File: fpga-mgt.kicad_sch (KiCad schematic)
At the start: 1 part, among them U1 XC7K410T-2FFG900I

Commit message: Loclib
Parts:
- U1: footprint antmicro-footprints:xc7k410t-2ffg900I -> K410T-devboard-footprints:xc7k410t-2ffg900I; symbol antmicroMicrocontrollers:XC7K410T-2FFG900I -> K410T-devboard:XC7K410T-2FFG900I

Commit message: Bump revision to 1.0.0. Update name on schematic and PCB sheets
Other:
- title: K410T devboard -> Kintex 410T devboard

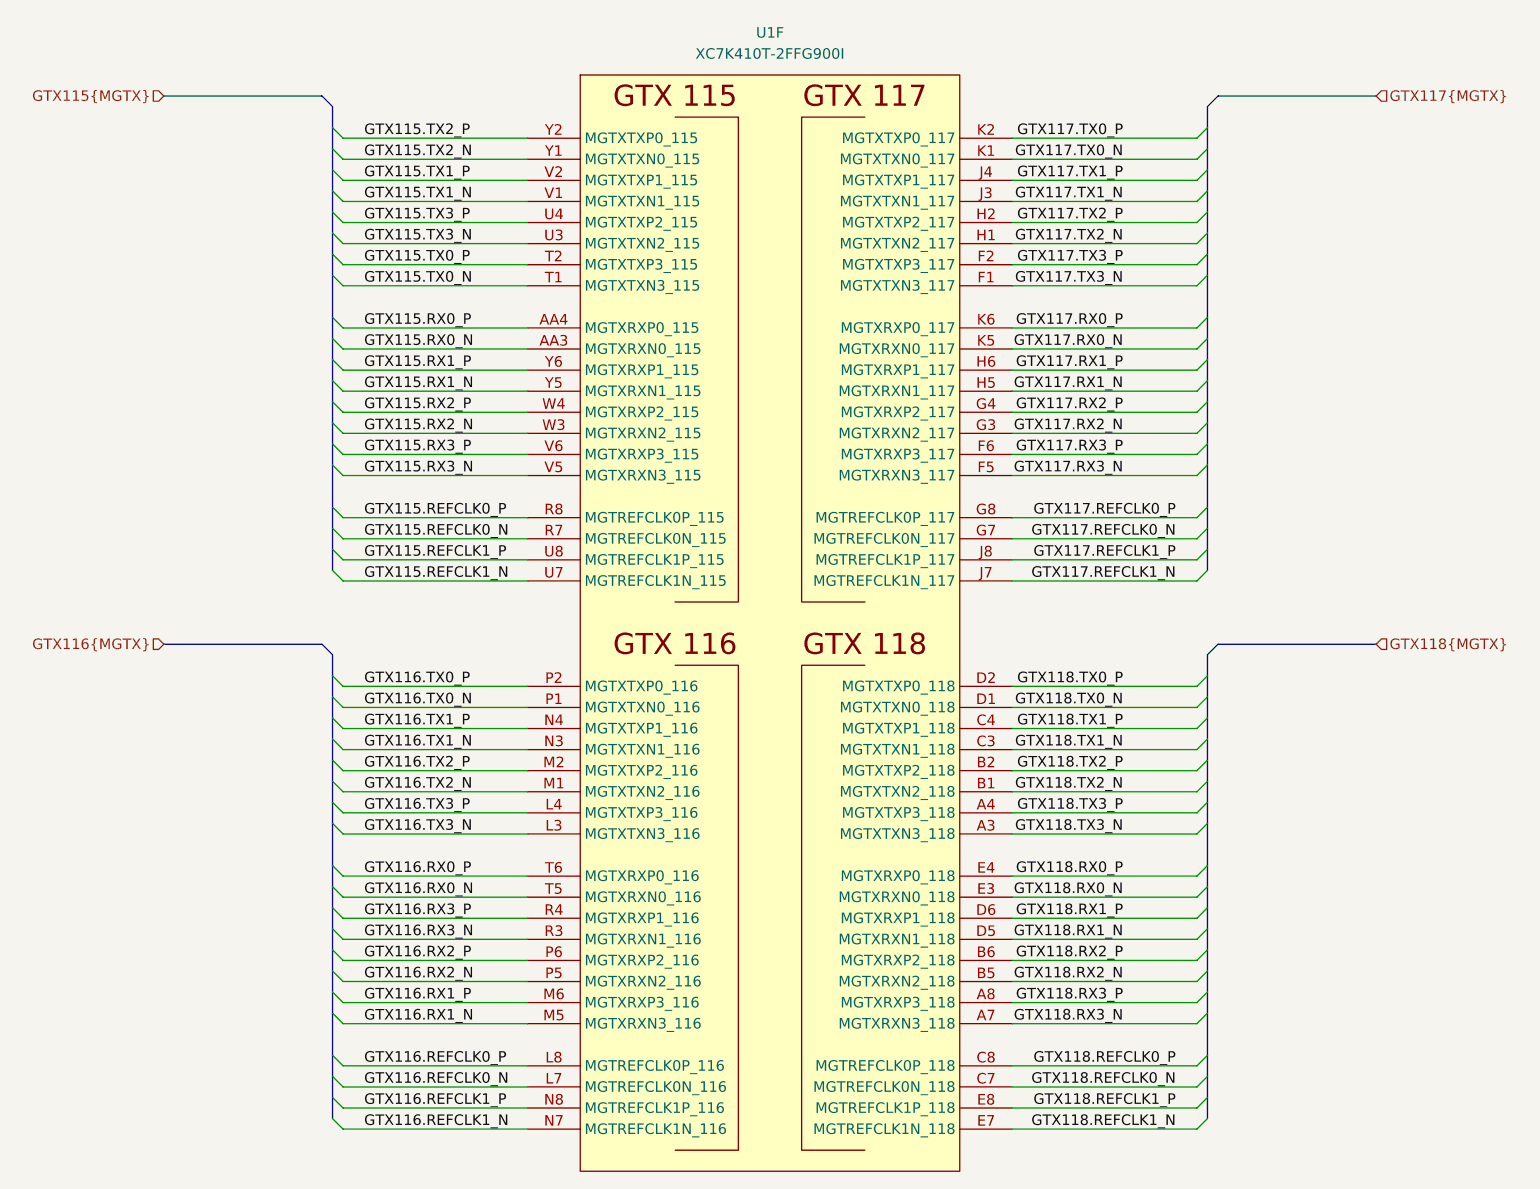
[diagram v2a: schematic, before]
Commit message: Introduce component standardization
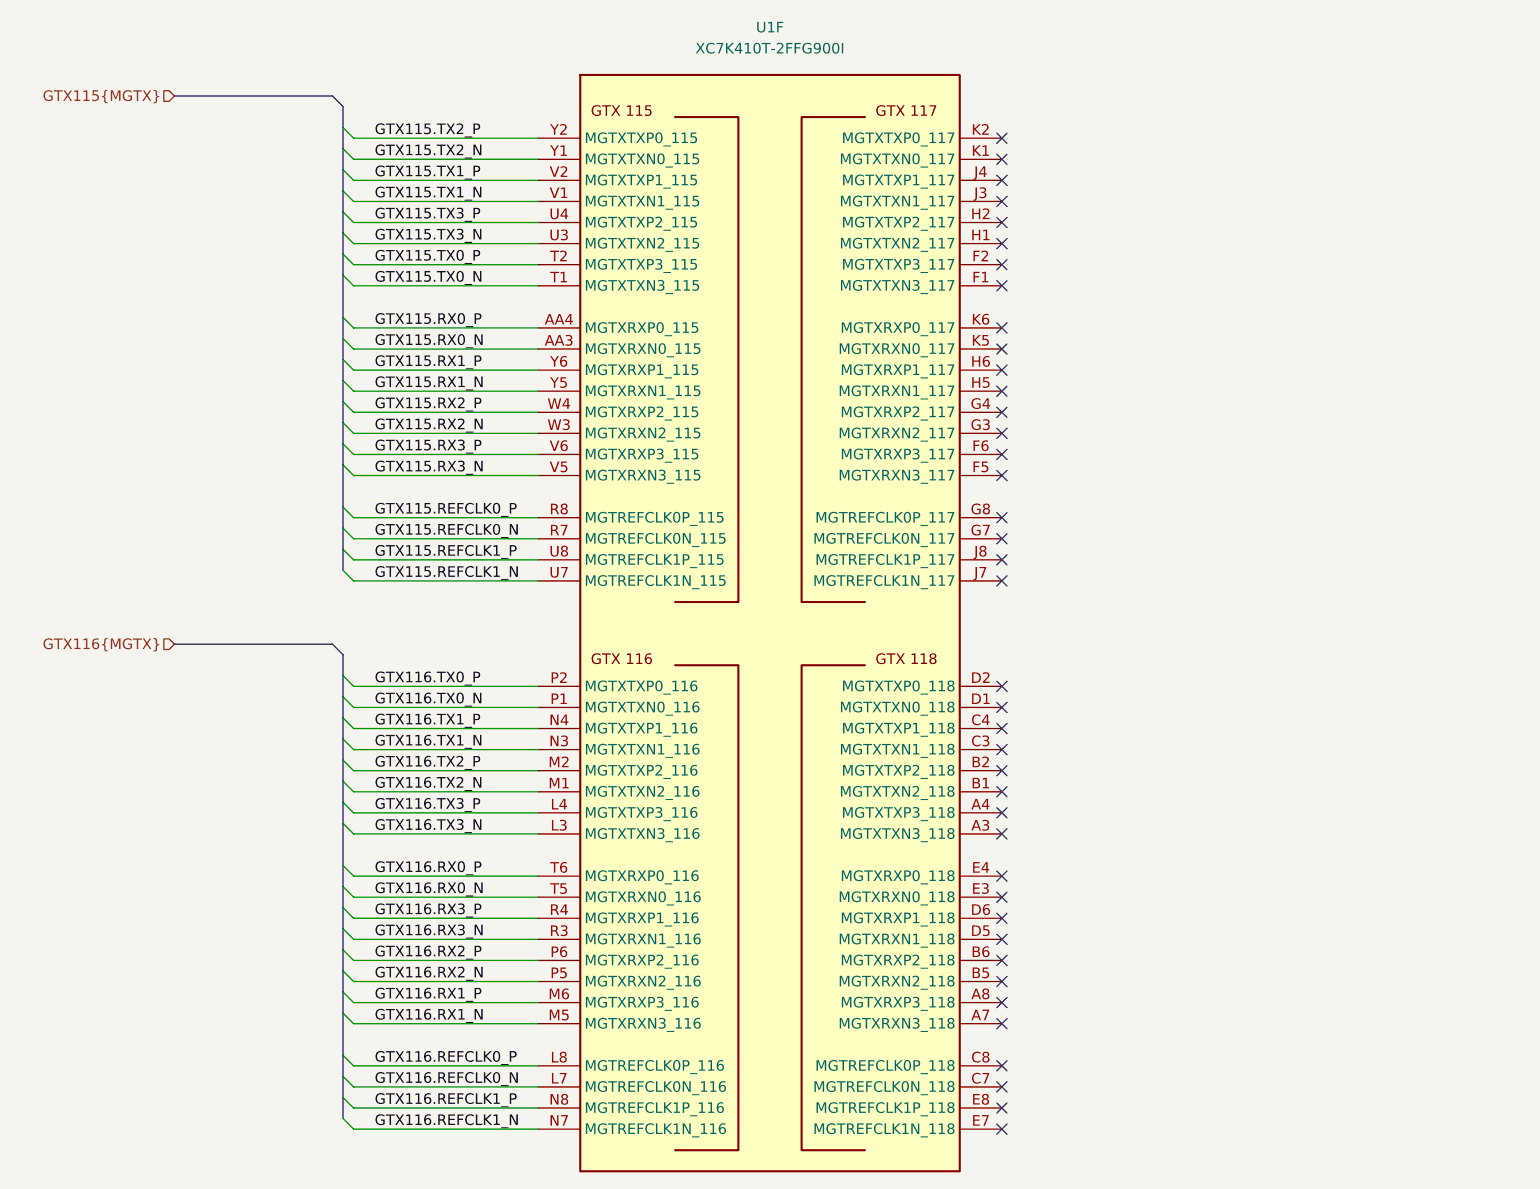
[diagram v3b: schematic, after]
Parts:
- U1: Author (none) -> Antmicro; License (none) -> Apache-2.0
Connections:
- net GTX117.REFCLK0_N: no longer names the net of U1.G7 (MGTREFCLK0N_117)
- net GTX117.REFCLK0_P: no longer names the net of U1.G8 (MGTREFCLK0P_117)
- net GTX117.REFCLK1_N: no longer names the net of U1.J7 (MGTREFCLK1N_117)
- net GTX117.REFCLK1_P: no longer names the net of U1.J8 (MGTREFCLK1P_117)
- net GTX117.RX0_N: no longer names the net of U1.K5 (MGTXRXN0_117)
- net GTX117.RX0_P: no longer names the net of U1.K6 (MGTXRXP0_117)
- net GTX117.RX1_N: no longer names the net of U1.H5 (MGTXRXN1_117)
- net GTX117.RX1_P: no longer names the net of U1.H6 (MGTXRXP1_117)
- net GTX117.RX2_N: no longer names the net of U1.G3 (MGTXRXN2_117)
- net GTX117.RX2_P: no longer names the net of U1.G4 (MGTXRXP2_117)
- net GTX117.RX3_N: no longer names the net of U1.F5 (MGTXRXN3_117)
- net GTX117.RX3_P: no longer names the net of U1.F6 (MGTXRXP3_117)
- net GTX117.TX0_N: no longer names the net of U1.K1 (MGTXTXN0_117)
- net GTX117.TX0_P: no longer names the net of U1.K2 (MGTXTXP0_117)
- net GTX117.TX1_N: no longer names the net of U1.J3 (MGTXTXN1_117)
- net GTX117.TX1_P: no longer names the net of U1.J4 (MGTXTXP1_117)
- net GTX117.TX2_N: no longer names the net of U1.H1 (MGTXTXN2_117)
- net GTX117.TX2_P: no longer names the net of U1.H2 (MGTXTXP2_117)
- net GTX117.TX3_N: no longer names the net of U1.F1 (MGTXTXN3_117)
- net GTX117.TX3_P: no longer names the net of U1.F2 (MGTXTXP3_117)
- net GTX118.REFCLK0_N: no longer names the net of U1.C7 (MGTREFCLK0N_118)
- net GTX118.REFCLK0_P: no longer names the net of U1.C8 (MGTREFCLK0P_118)
- net GTX118.REFCLK1_N: no longer names the net of U1.E7 (MGTREFCLK1N_118)
- net GTX118.REFCLK1_P: no longer names the net of U1.E8 (MGTREFCLK1P_118)
- net GTX118.RX0_N: no longer names the net of U1.E3 (MGTXRXN0_118)
- net GTX118.RX0_P: no longer names the net of U1.E4 (MGTXRXP0_118)
- net GTX118.RX1_N: no longer names the net of U1.D5 (MGTXRXN1_118)
- net GTX118.RX1_P: no longer names the net of U1.D6 (MGTXRXP1_118)
- net GTX118.RX2_N: no longer names the net of U1.B5 (MGTXRXN2_118)
- net GTX118.RX2_P: no longer names the net of U1.B6 (MGTXRXP2_118)
- net GTX118.RX3_N: no longer names the net of U1.A7 (MGTXRXN3_118)
- net GTX118.RX3_P: no longer names the net of U1.A8 (MGTXRXP3_118)
- net GTX118.TX0_N: no longer names the net of U1.D1 (MGTXTXN0_118)
- net GTX118.TX0_P: no longer names the net of U1.D2 (MGTXTXP0_118)
- net GTX118.TX1_N: no longer names the net of U1.C3 (MGTXTXN1_118)
- net GTX118.TX1_P: no longer names the net of U1.C4 (MGTXTXP1_118)
- net GTX118.TX2_N: no longer names the net of U1.B1 (MGTXTXN2_118)
- net GTX118.TX2_P: no longer names the net of U1.B2 (MGTXTXP2_118)
- net GTX118.TX3_N: no longer names the net of U1.A3 (MGTXTXN3_118)
- net GTX118.TX3_P: no longer names the net of U1.A4 (MGTXTXP3_118)
- no-connect marks 0 -> 40

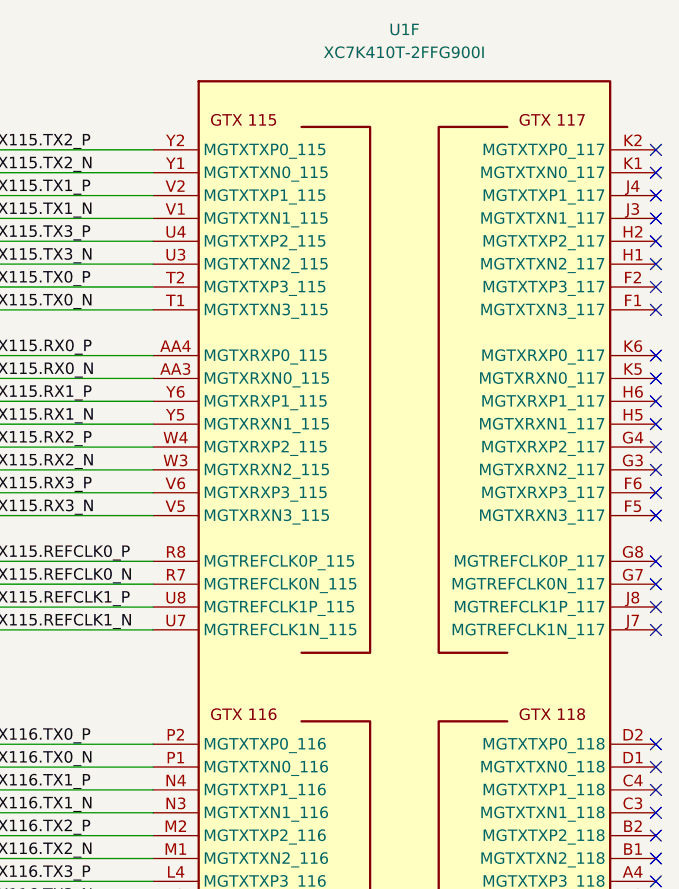
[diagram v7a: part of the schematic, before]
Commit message: [#55729] Change Manufacturer to AMD-Xilinx
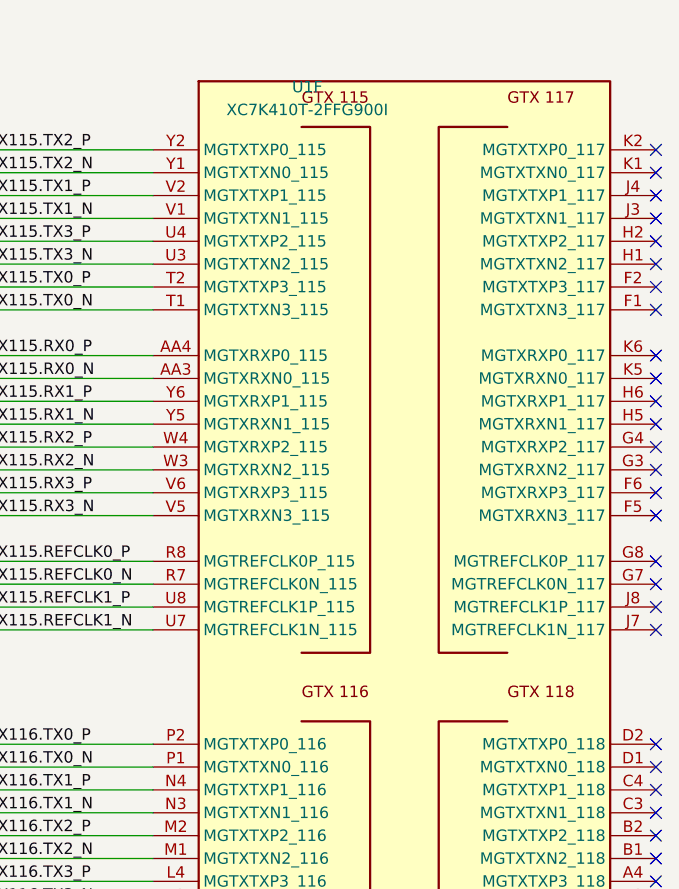
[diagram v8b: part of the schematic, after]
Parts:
- U1: Manufacturer Xilinx -> AMD-Xilinx
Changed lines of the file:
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@@
   (symbol (lib_id "K410T-devboard:XC7K410T-2FFG900I") (at 172.085 78.74 0) (unit 6)
     (in_bom yes) (on_board yes) (dnp no) (fields_autoplaced)
-    (property "Reference" "U1" (at 200.025 65.405 0)
+    (property "Reference" "U1" (at 189.23 71.755 0)
       (effects (font (size 1.27 1.27) (thickness 0.15)))
     )
-    (property "Value" "XC7K410T-2FFG900I" (at 200.025 67.945 0)
+    (property "Value" "XC7K410T-2FFG900I" (at 189.23 74.295 0)
       (effects (font (size 1.27 1.27) (thickness 0.15)))
     )
@@
       (effects (font (size 1.27 1.27) (thickness 0.15)) (justify left bottom) hide)
     )
-    (property "Manufacturer" "Xilinx" (at 172.085 57.15 0)
+    (property "Manufacturer" "AMD-Xilinx" (at 172.085 57.15 0)
       (effects (font (size 1.27 1.27) (thickness 0.15)) (justify left bottom) hide)
     )
@@
           (reference "U1") (unit 6)
         )
+        (path "/c1489e7c-896d-4046-acd4-3929998e87dc/020031b8-7f27-4e26-b74c-26be7f0881a9"
+          (reference "U1") (unit 6)
+        )
